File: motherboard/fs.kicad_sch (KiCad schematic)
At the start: 87 parts, among them J101 Header, J102 640389-2, Q101 MJD44H11, Q102 MJD45H11, U101 INA132UA, U102 LM741C, U103 LMH6609, U104 LM317, U105 LM337, U106 LM340-5, U107 MC7905ACD2T

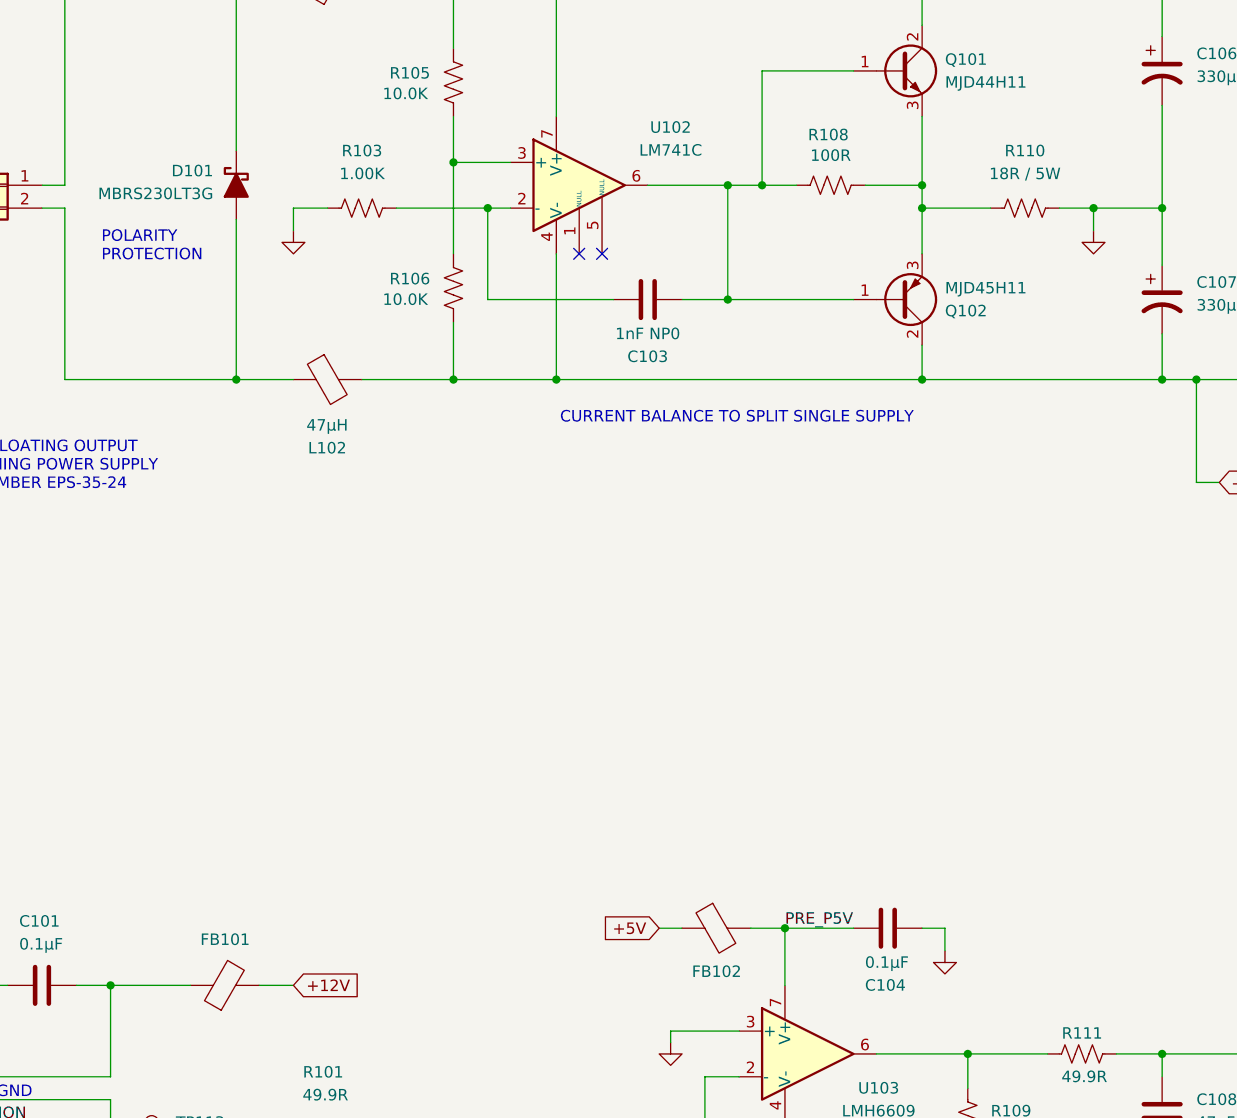
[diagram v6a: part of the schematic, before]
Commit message: update bead value for ocxo power
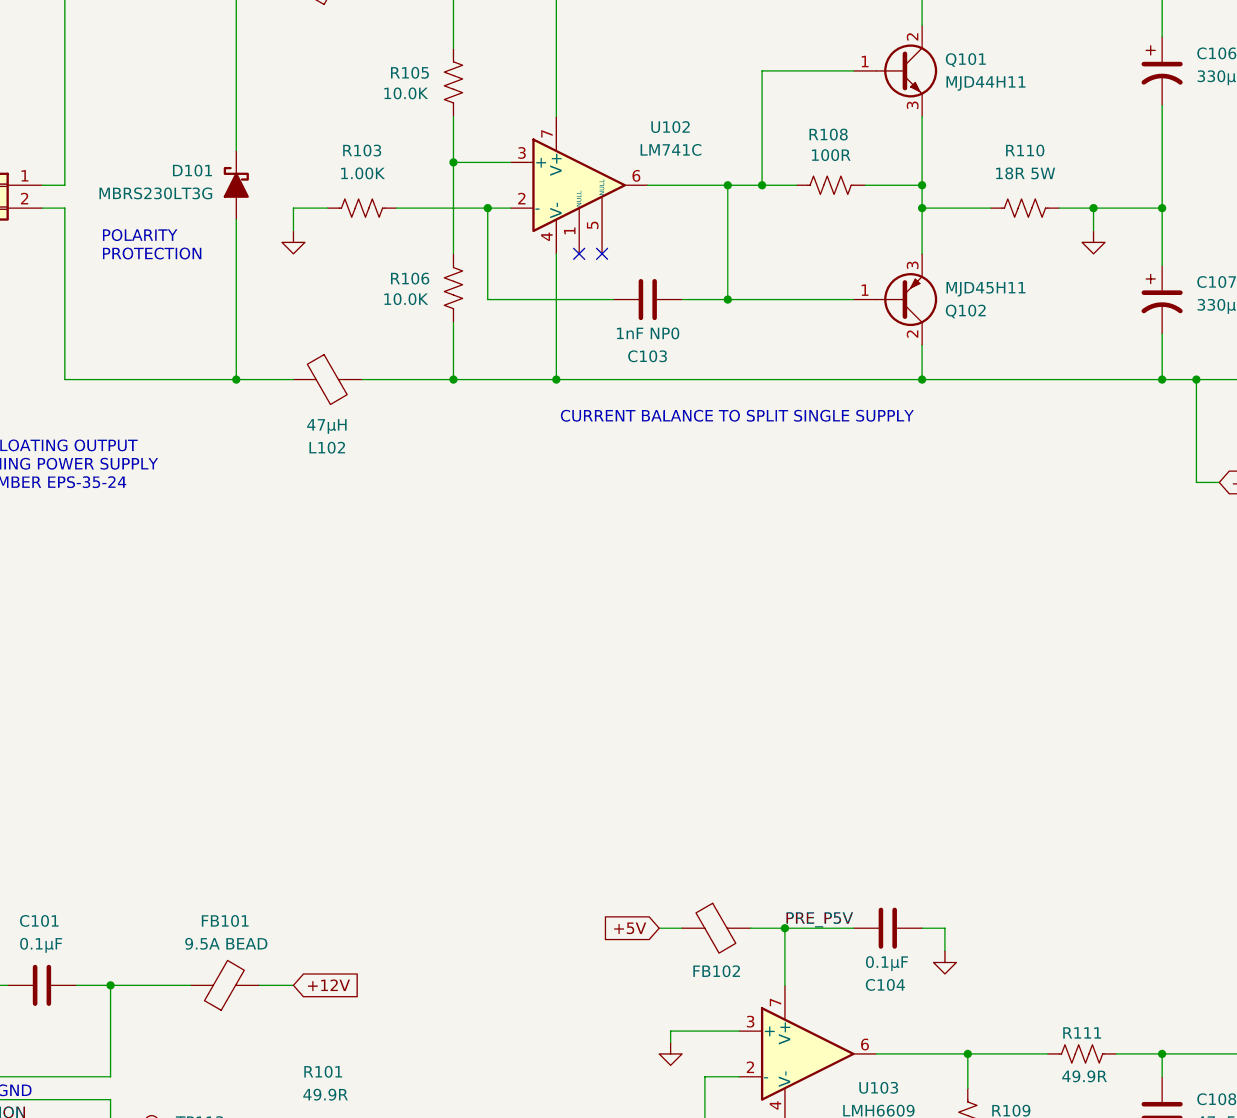
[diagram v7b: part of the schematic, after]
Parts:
- FB101: value 742863160 -> 9.5A BEAD
- R110: value 18R / 5W -> 18R 5W
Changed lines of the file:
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@@
 		(dnp no)
 		(property "Reference" "FB101"
-			(at 80.264 146.05 90)
-			(show_name no)
-			(do_not_autoplace no)
-			(effects
-				(font
-					(size 1.27 1.27)
-				)
-				(justify left)
-			)
-		)
-		(property "Value" "742863160"
-			(at 78.6891 147.32 0)
-			(hide yes)
+			(at 80.264 144.018 90)
+			(show_name no)
+			(do_not_autoplace no)
+			(effects
+				(font
+					(size 1.27 1.27)
+				)
+				(justify left)
+			)
+		)
+		(property "Value" "9.5A BEAD"
+			(at 82.296 146.558 90)
 			(show_name no)
 			(do_not_autoplace no)
@@
 			)
 		)
-		(property "Value" "18R / 5W"
+		(property "Value" "18R 5W"
 			(at 166.37 60.96 90)
 			(show_name no)

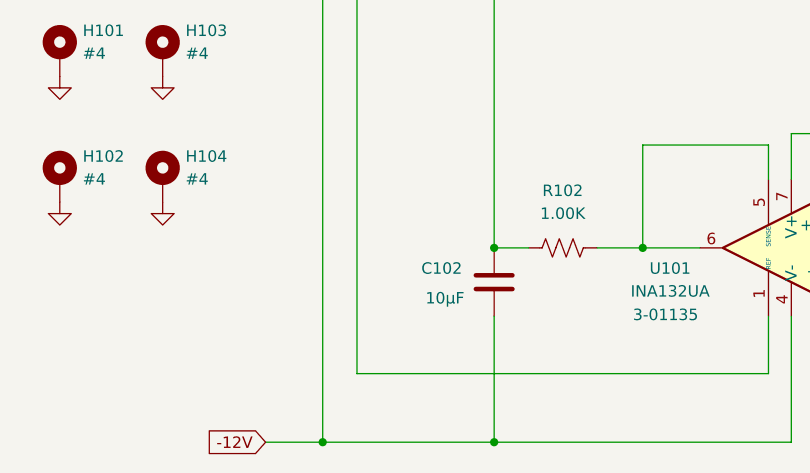
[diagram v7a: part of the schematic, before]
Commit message: make FREQ_CTL filter cap an NP0 part
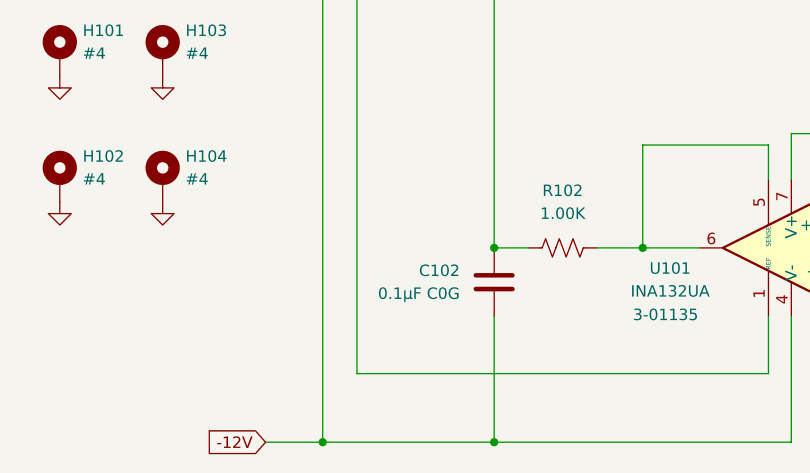
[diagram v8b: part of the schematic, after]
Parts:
- removed C102: 10μF, Capacitor_SMD:C_0805_2012Metric, symbol #SRS:5_Capacitors/5-00954
- added C102: 0.1μF C0G, Capacitor_SMD:C_1206_3216Metric, symbol #SRS:5_Capacitors/5-01075
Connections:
- net -12V: now also C102.2
- net FREQ_CTL: now also C102.1
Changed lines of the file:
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@@
 	)
 	(junction
+		(at 83.82 227.33)
+		(diameter 0)
+		(color 0 0 0 0)
+	)
+	(junction
 		(at 215.9 52.07)
 		(diameter 0)
@@
 	)
 	(junction
-		(at 83.82 227.33)
-		(diameter 0)
-		(color 0 0 0 0)
-	)
-	(junction
 		(at 181.61 158.75)
 		(diameter 0)
@@
 	)
 	(symbol
+		(lib_id "#SRS:5_Capacitors/5-01075")
+		(at 83.82 231.14 0)
+		(mirror y)
+		(unit 1)
+		(body_style 1)
+		(exclude_from_sim no)
+		(in_bom yes)
+		(on_board yes)
+		(in_pos_files yes)
+		(dnp no)
+		(property "Reference" "C102"
+			(at 80.01 229.8699 0)
+			(show_name no)
+			(do_not_autoplace no)
+			(effects
+				(font
+					(size 1.27 1.27)
+				)
+				(justify left)
+			)
+		)
+		(property "Value" "0.1μF C0G"
+			(at 80.01 232.4099 0)
+			(show_name no)
+			(do_not_autoplace no)
+			(effects
+				(font
+					(size 1.27 1.27)
+				)
+				(justify left)
+			)
+		)
+		(property "Footprint" "Capacitor_SMD:C_1206_3216Metric"
+			(at 82.8548 234.95 0)
+			(hide yes)
+			(show_name no)
+			(do_not_autoplace no)
+			(effects
+				(font
+					(size 1.27 1.27)
+				)
+			)
+		)
+		(property "Datasheet" ""
+			(at 83.82 231.14 0)
+			(hide yes)
+			(show_name no)
+			(do_not_autoplace no)
+			(effects
+				(font
+					(size 1.27 1.27)
+				)
+			)
+		)
+		(property "Description" "Cap Ceramic 0.1uF 50V C0G 1% Pad SMD 1206 125°C Automotive AEC-Q200 T/R"
+			(at 83.82 231.14 0)
+			(hide yes)
+			(show_name no)
+			(do_not_autoplace no)
+			(effects
+				(font
+					(size 1.27 1.27)
+				)
+			)
+		)
+		(property "SRS PN" "5-01075"
+			(at 83.82 231.14 0)
+			(hide yes)
+			(show_name no)
+			(do_not_autoplace no)
+			(effects
+				(font
+					(size 1.27 1.27)
+				)
+			)
+		)
+		(property "MPN" "GRT31C5C1H104FA02L"
+			(at 83.82 231.14 0)
+			(hide yes)
+			(show_name no)
+			(do_not_autoplace no)
+			(effects
+				(font
+					(size 1.27 1.27)
+				)
+			)
+		)
+		(property "Voltage" "50V"
+			(at 83.82 231.14 0)
+			(hide yes)
+			(show_name no)
+			(do_not_autoplace no)
+			(effects
+				(font
+					(size 1.27 1.27)
+				)
+			)
+		)
+		(property "JLCPCB" "C3839854"
+			(at 83.82 231.14 0)
+			(hide yes)
+			(show_name no)
+			(do_not_autoplace no)
+			(effects
+				(font
+					(size 1.27 1.27)
+				)
+			)
+		)
+		(pin "1"
+		)
+		(pin "2"
+		)
+		(instances
+			(project "fs"
+				(path "/8ffb403b-c4c8-4a5b-a7cd-53604dae5dc0"
+					(reference "C102")
+					(unit 1)
+				)
+			)
+		)
+	)
+	(symbol
 		(lib_id "Mechanical:MountingHole_Pad")
 		(at 46.99 205.74 0)
@@
 					(unit 1)
 				)
-			)
-		)
-	)
-	(symbol
-		(lib_id "#SRS:5_Capacitors/5-00954")
-		(at 83.82 231.14 0)
-		(mirror y)
-		(unit 1)
-		(body_style 1)
-		(exclude_from_sim no)
-		(in_bom yes)
-		(on_board yes)
-		(in_pos_files yes)
-		(dnp no)
-		(property "Reference" "C102"
-			(at 80.264 229.616 0)
-			(show_name no)
-			(do_not_autoplace no)
-			(effects
-				(font
-					(size 1.27 1.27)
-				)
-				(justify left)
-			)
-		)
-		(property "Value" "10μF"
-			(at 80.518 232.918 0)
-			(show_name no)
-			(do_not_autoplace no)
-			(effects
-				(font
-					(size 1.27 1.27)
-				)
-				(justify left)
-			)
-		)
-		(property "Footprint" "Capacitor_SMD:C_0805_2012Metric"
-			(at 82.8548 234.95 0)
-			(hide yes)
-			(show_name no)
-			(do_not_autoplace no)
-			(effects
-				(font
-					(size 1.27 1.27)
-				)
-			)
-		)
-		(property "Datasheet" ""
-			(at 83.82 231.14 0)
-			(hide yes)
-			(show_name no)
-			(do_not_autoplace no)
-			(effects
-				(font
-					(size 1.27 1.27)
-				)
-			)
-		)
-		(property "Description" "10 uF 0805 capacitor, 25V X5R 10%"
-			(at 83.82 231.14 0)
-			(hide yes)
-			(show_name no)
-			(do_not_autoplace no)
-			(effects
-				(font
-					(size 1.27 1.27)
-				)
-			)
-		)
-		(property "SRS PN" "5-00954"
-			(at 83.82 231.14 0)
-			(hide yes)
-			(show_name no)
-			(do_not_autoplace no)
-			(effects
-				(font
-					(size 1.27 1.27)
-				)
-			)
-		)
-		(property "Voltage" "25V"
-			(at 83.82 231.14 0)
-			(hide yes)
-			(show_name no)
-			(do_not_autoplace no)
-			(effects
-				(font
-					(size 1.27 1.27)
-				)
-			)
-		)
-		(property "MPN" "GRM21BR61E106KA73L"
-			(at 83.82 231.14 0)
-			(hide yes)
-			(show_name no)
-			(do_not_autoplace no)
-			(effects
-				(font
-					(size 1.27 1.27)
-				)
-			)
-		)
-		(property "JLCPCB" "C84416"
-			(at 83.82 231.14 0)
-			(hide yes)
-			(show_name no)
-			(do_not_autoplace no)
-			(effects
-				(font
-					(size 1.27 1.27)
-				)
-			)
-		)
-		(pin "2"
-		)
-		(pin "1"
-		)
-		(instances
-			(project "fs"
-				(path "/8ffb403b-c4c8-4a5b-a7cd-53604dae5dc0"
-					(reference "C102")
-					(unit 1)
-				)
